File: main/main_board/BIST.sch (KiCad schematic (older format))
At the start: 20 parts, among them M1 microzed, U8 DAC80004IPW, U9 74LVC541A

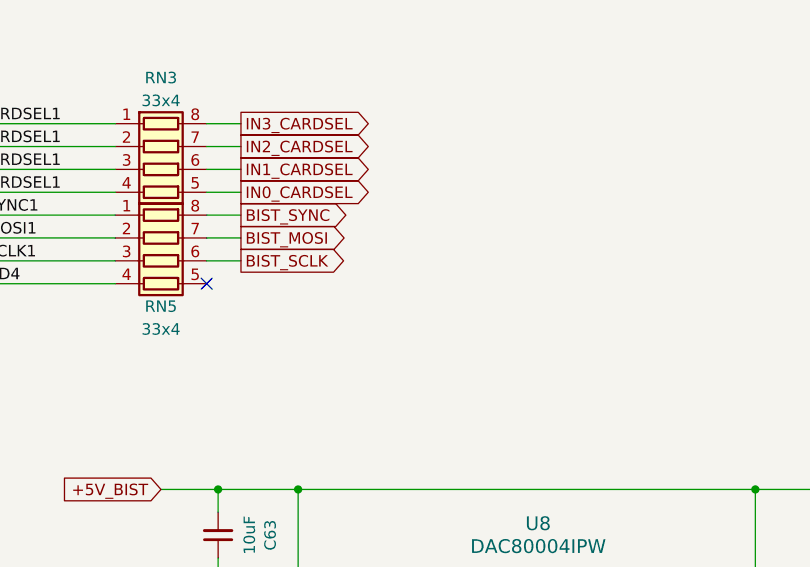
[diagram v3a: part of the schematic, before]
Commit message: Added testpoints, debug IO port, LEDs, and clock output jack.
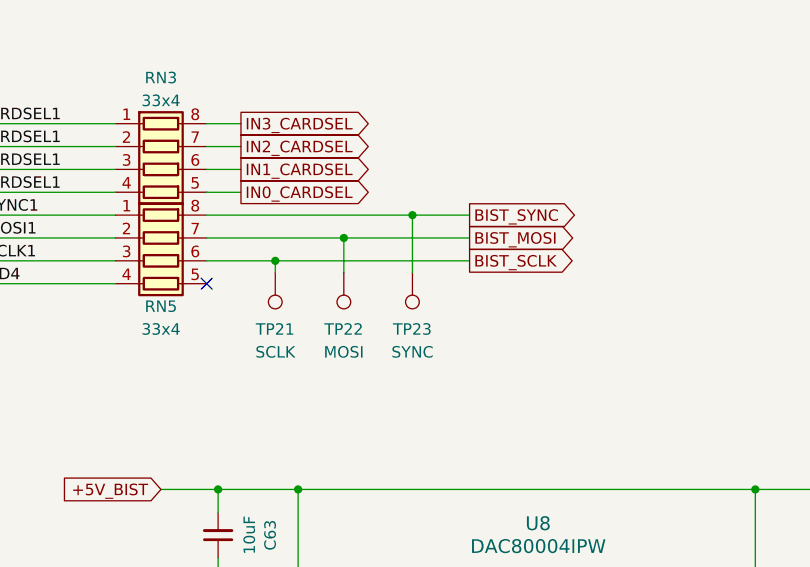
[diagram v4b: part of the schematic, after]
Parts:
- added TP21: SCLK, TestPoint:TestPoint_Keystone_5000-5004_Miniature, symbol Connector:TestPoint
- added TP22: MOSI, TestPoint:TestPoint_Keystone_5000-5004_Miniature, symbol Connector:TestPoint
- added TP23: SYNC, TestPoint:TestPoint_Keystone_5000-5004_Miniature, symbol Connector:TestPoint
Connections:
- net BIST_MOSI: now also TP22.1
- net BIST_SCLK: now also TP21.1
- net BIST_SYNC: now also TP23.1
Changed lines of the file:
@@
 	2550 2400 2550 2600
 Connection ~ 2550 2600
-Text GLabel 5000 2100 2    50   Output ~ 0
+Text GLabel 6000 2100 2    50   Output ~ 0
 BIST_SYNC
-Text GLabel 5000 2200 2    50   Output ~ 0
+Text GLabel 6000 2200 2    50   Output ~ 0
 BIST_MOSI
-Text GLabel 5000 2300 2    50   Output ~ 0
+Text GLabel 6000 2300 2    50   Output ~ 0
 BIST_SCLK
-Wire Wire Line
-	5000 2100 4850 2100
-Wire Wire Line
-	5000 2200 4850 2200
-Wire Wire Line
-	5000 2300 4850 2300
 $Comp
 L microzed:microzed M1
@@
 Text GLabel 5000 1900 2    50   Output ~ 0
 IN1_CARDSEL
+Wire Wire Line
+	4850 2100 5750 2100
+Wire Wire Line
+	4850 2200 5450 2200
+Wire Wire Line
+	4850 2300 5150 2300
+$Comp
+L Connector:TestPoint TP?
+U 1 1 5F17567E
+P 5150 2350
+AR Path="/5DFCF14D/5DA78AA2/5F17567E" Ref="TP?"  Part="1"
+AR Path="/5DFCF14D/5E295469/5F17567E" Ref="TP?"  Part="1"
+AR Path="/5DFCF14D/5E195558/5F17567E" Ref="TP?"  Part="1"
+AR Path="/5F17567E" Ref="TP?"  Part="1"
+AR Path="/5E525FC9/5F17567E" Ref="TP?"  Part="1"
+AR Path="/5EC4BDFA/5F17567E" Ref="TP21"  Part="1"
+F 0 "TP21" H 5150 2600 50  0000 C CNN
+F 1 "SCLK" H 5150 2700 50  0000 C CNN
+F 2 "TestPoint:TestPoint_Keystone_5000-5004_Miniature" H 5350 2350 50  0001 C CNN
+F 3 "~" H 5350 2350 50  0001 C CNN
+F 4 "Do Not Populate" H 5150 2350 50  0001 C CNN "Description"
+F 5 "DNP" H 5150 2350 50  0001 C CNN "MPN"
+	1    5150 2350
+	-1   0    0    1
+$EndComp
+$Comp
+L Connector:TestPoint TP?
+U 1 1 5F178BFC
+P 5450 2350
+AR Path="/5DFCF14D/5DA78AA2/5F178BFC" Ref="TP?"  Part="1"
+AR Path="/5DFCF14D/5E295469/5F178BFC" Ref="TP?"  Part="1"
+AR Path="/5DFCF14D/5E195558/5F178BFC" Ref="TP?"  Part="1"
+AR Path="/5F178BFC" Ref="TP?"  Part="1"
+AR Path="/5E525FC9/5F178BFC" Ref="TP?"  Part="1"
+AR Path="/5EC4BDFA/5F178BFC" Ref="TP22"  Part="1"
+F 0 "TP22" H 5450 2600 50  0000 C CNN
+F 1 "MOSI" H 5450 2700 50  0000 C CNN
+F 2 "TestPoint:TestPoint_Keystone_5000-5004_Miniature" H 5650 2350 50  0001 C CNN
+F 3 "~" H 5650 2350 50  0001 C CNN
+F 4 "Do Not Populate" H 5450 2350 50  0001 C CNN "Description"
+F 5 "DNP" H 5450 2350 50  0001 C CNN "MPN"
+	1    5450 2350
+	-1   0    0    1
+$EndComp
+$Comp
+L Connector:TestPoint TP?
+U 1 1 5F17C309
+P 5750 2350
+AR Path="/5DFCF14D/5DA78AA2/5F17C309" Ref="TP?"  Part="1"
+AR Path="/5DFCF14D/5E295469/5F17C309" Ref="TP?"  Part="1"
+AR Path="/5DFCF14D/5E195558/5F17C309" Ref="TP?"  Part="1"
+AR Path="/5F17C309" Ref="TP?"  Part="1"
+AR Path="/5E525FC9/5F17C309" Ref="TP?"  Part="1"
+AR Path="/5EC4BDFA/5F17C309" Ref="TP23"  Part="1"
+F 0 "TP23" H 5750 2600 50  0000 C CNN
+F 1 "SYNC" H 5750 2700 50  0000 C CNN
+F 2 "TestPoint:TestPoint_Keystone_5000-5004_Miniature" H 5950 2350 50  0001 C CNN
+F 3 "~" H 5950 2350 50  0001 C CNN
+F 4 "Do Not Populate" H 5750 2350 50  0001 C CNN "Description"
+F 5 "DNP" H 5750 2350 50  0001 C CNN "MPN"
+	1    5750 2350
+	-1   0    0    1
+$EndComp
+Wire Wire Line
+	5150 2350 5150 2300
+Connection ~ 5150 2300
+Wire Wire Line
+	5150 2300 6000 2300
+Wire Wire Line
+	5450 2350 5450 2200
+Connection ~ 5450 2200
+Wire Wire Line
+	5450 2200 6000 2200
+Wire Wire Line
+	5750 2350 5750 2100
+Connection ~ 5750 2100
+Wire Wire Line
+	5750 2100 6000 2100
 $EndSCHEMATC

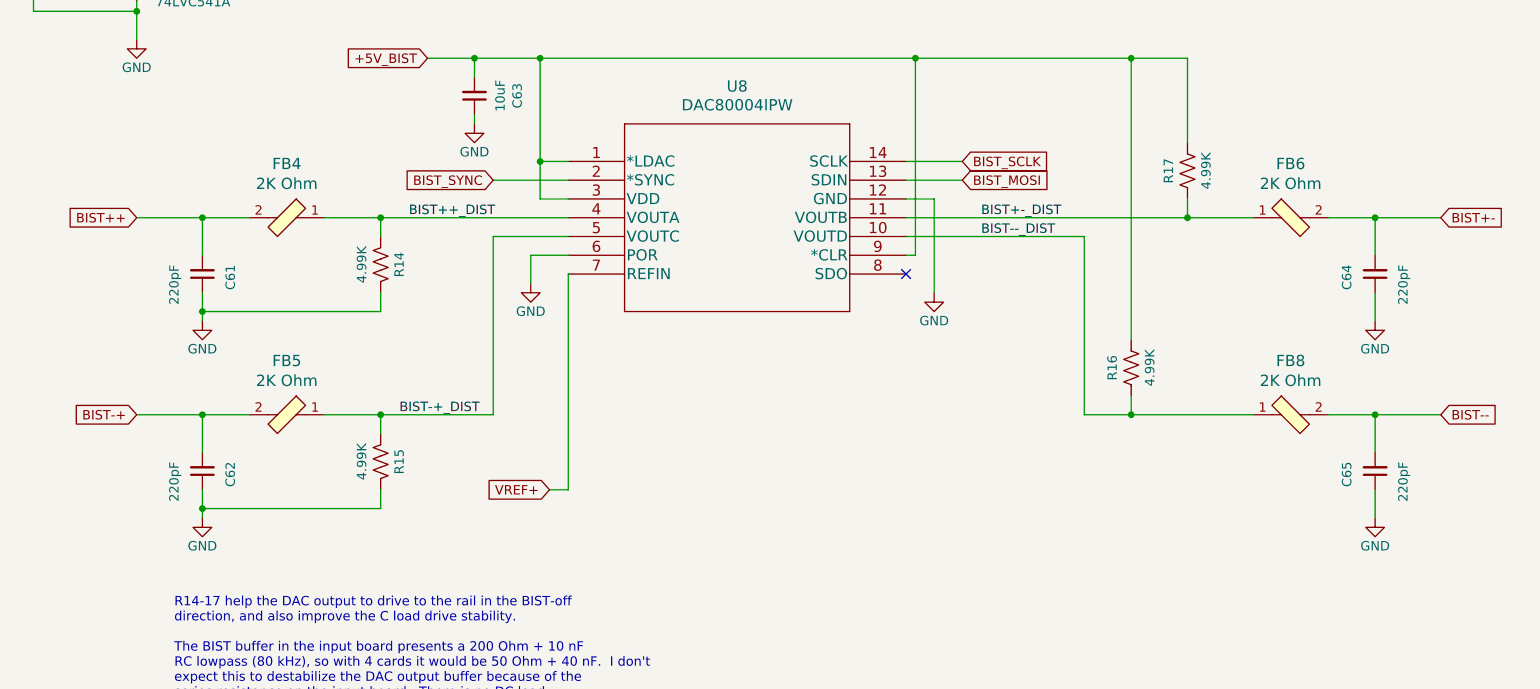
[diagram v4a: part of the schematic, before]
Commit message: Finishing up main/main_board/main_board.kicad_pcb.  Test points, stiching vias, ground pours.
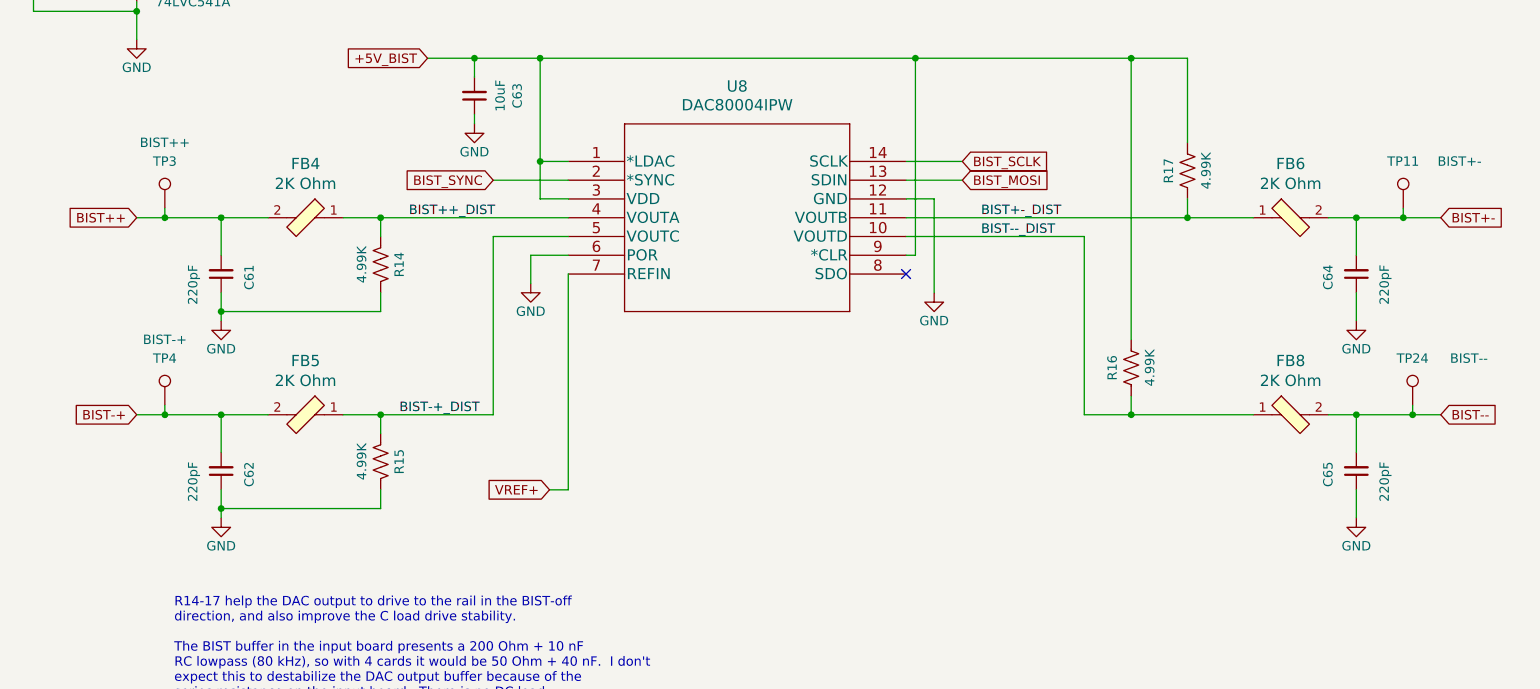
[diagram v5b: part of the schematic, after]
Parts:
- added TP11: BIST+-, TestPoint:TestPoint_Keystone_5000-5004_Miniature, symbol Connector:TestPoint
- added TP24: BIST--, TestPoint:TestPoint_Keystone_5000-5004_Miniature, symbol Connector:TestPoint
- added TP3: BIST++, TestPoint:TestPoint_Keystone_5000-5004_Miniature, symbol Connector:TestPoint
- added TP4: BIST-+, TestPoint:TestPoint_Keystone_5000-5004_Miniature, symbol Connector:TestPoint
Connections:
- net BIST++: now also TP3.1
- net BIST+-: now also TP11.1
- net BIST-+: now also TP4.1
- net BIST--: now also TP24.1
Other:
- moved on the sheet: C61, C62, C64, C65, FB4, FB5

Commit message: Main board seems to be about ready to be set off. Added gerber files. Made new footprints for the LEDs and DAC, since nothing in the standard footprints was a good match for the manufacturer recommended pattern. Moved around component values on the fab layer. Tweaked ground plane thermal via and fill width so that we get continuity between pins on the PCIe connectors. Moved OVDD vias to also avoid ground plane slotting. Added local copper pours on planes on U6 thermal pad to prevent thermal reliefs on the thermal vias.
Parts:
- U8: footprint Package_SO:SSOP-14_5.3x6.2mm_P0.65mm -> main_board:TI_R_PDSO_G14
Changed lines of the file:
@@
 F 0 "U8" H 6300 4250 60  0000 C CNN
 F 1 "DAC80004IPW" H 6300 4150 60  0000 C CNN
-F 2 "Package_SO:SSOP-14_5.3x6.2mm_P0.65mm" H 6300 4090 60  0001 C CNN
+F 2 "main_board:TI_R_PDSO_G14" H 6300 4090 60  0001 C CNN
 F 3 "http://www.ti.com/general/docs/suppproductinfo.tsp?distId=10&gotoUrl=http%3A%2F%2Fwww.ti.com%2Flit%2Fgpn%2Fdac60004" H 5400 3850 60  0001 C CNN
 F 4 "IC DAC 16BIT V-OUT 14TSSOP" H 5400 3850 50  0001 C CNN "Description"

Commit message: I added a bypass cap on the BIST DAC reference input. Though not required on the datasheet, it seems like a good idea because the bandwidth at the reference input is 350 kHz.
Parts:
- added C76: 10uF, Capacitor_SMD:C_0603_1608Metric, symbol Device:C_Small
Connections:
- net GND: now also C76.1
- net VREF+: now also C76.2
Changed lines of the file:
@@
 Wire Wire Line
 	3550 5700 3550 5750
-Text GLabel 5300 5600 0    50   Input ~ 0
+Text GLabel 5700 5050 2    50   Input ~ 0
 VREF+
-Wire Wire Line
-	5300 5600 5400 5600
-Wire Wire Line
-	5400 5600 5400 4450
 Text GLabel 5000 3950 0    50   Input ~ 0
 BIST_SYNC
@@
 	1    0    0    -1
 $EndComp
+$Comp
+L power:GND #PWR?
+U 1 1 5F421C03
+P 5400 5450
+AR Path="/5E624B3C/5E51E83D/5F421C03" Ref="#PWR?"  Part="1"
+AR Path="/5E525F2C/5F421C03" Ref="#PWR?"  Part="1"
+AR Path="/5E525FC9/5F421C03" Ref="#PWR?"  Part="1"
+AR Path="/5EC4BDFA/5F421C03" Ref="#PWR0137"  Part="1"
+F 0 "#PWR0137" H 5400 5200 50  0001 C CNN
+F 1 "GND" H 5400 5300 50  0000 C CNN
+F 2 "" H 5400 5450 50  0001 C CNN
+F 3 "" H 5400 5450 50  0001 C CNN
+	1    5400 5450
+	1    0    0    -1
+$EndComp
+Wire Wire Line
+	5400 5400 5400 5450
+$Comp
+L Device:C_Small C?
+U 1 1 5F421C0F
+P 5400 5300
+AR Path="/5DFF6C0D/5F421C0F" Ref="C?"  Part="1"
+AR Path="/5E1D6729/5E1DA2AA/5F421C0F" Ref="C?"  Part="1"
+AR Path="/5E2EB92B/5F421C0F" Ref="C?"  Part="1"
+AR Path="/5E51E83D/5F421C0F" Ref="C?"  Part="1"
+AR Path="/5E624B3C/5E51E83D/5F421C0F" Ref="C?"  Part="1"
+AR Path="/5E525F2C/5F421C0F" Ref="C?"  Part="1"
+AR Path="/5E525FC9/5F421C0F" Ref="C?"  Part="1"
+AR Path="/5EC4BDFA/5F421C0F" Ref="C76"  Part="1"
+F 0 "C76" V 5171 5300 50  0000 C CNN
+F 1 "10uF" V 5262 5300 50  0000 C CNN
+F 2 "Capacitor_SMD:C_0603_1608Metric" H 5400 5300 50  0001 C CNN
+F 3 "http://datasheets.avx.com/cx5r.pdf" H 5400 5300 50  0001 C CNN
+F 4 "CAP CER 10UF 6.3V X5R 0603" H 5400 5300 50  0001 C CNN "Description"
+F 5 "478-5318-1-ND" H 5400 5300 50  0001 C CNN "Digikey"
+F 6 "06036D106MAT2A" H 5400 5300 50  0001 C CNN "MPN"
+F 7 "20" H 5400 5300 50  0001 C CNN "DK line"
+F 8 "AVX" H 5400 5300 50  0001 C CNN "Manufacturer"
+	1    5400 5300
+	-1   0    0    1
+$EndComp
+Wire Wire Line
+	5400 4450 5400 5050
+Wire Wire Line
+	5700 5050 5400 5050
+Connection ~ 5400 5050
+Wire Wire Line
+	5400 5050 5400 5200
 $EndSCHEMATC
